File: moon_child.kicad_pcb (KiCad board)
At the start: 4 copper layers, 63.2 x 63.2 mm, 186 parts, among them J1 Motor0, J10 USB_C_Receptacle_USB2.0_14P, J2 Motor1, J3 Battery Input, J4 Micro_SD_Card_Det1, J5 Conn_01x04, J6 Conn_01x04, J7 Conn_02x05_Odd_Even, J8 Conn_01x03, J9 debug_probe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

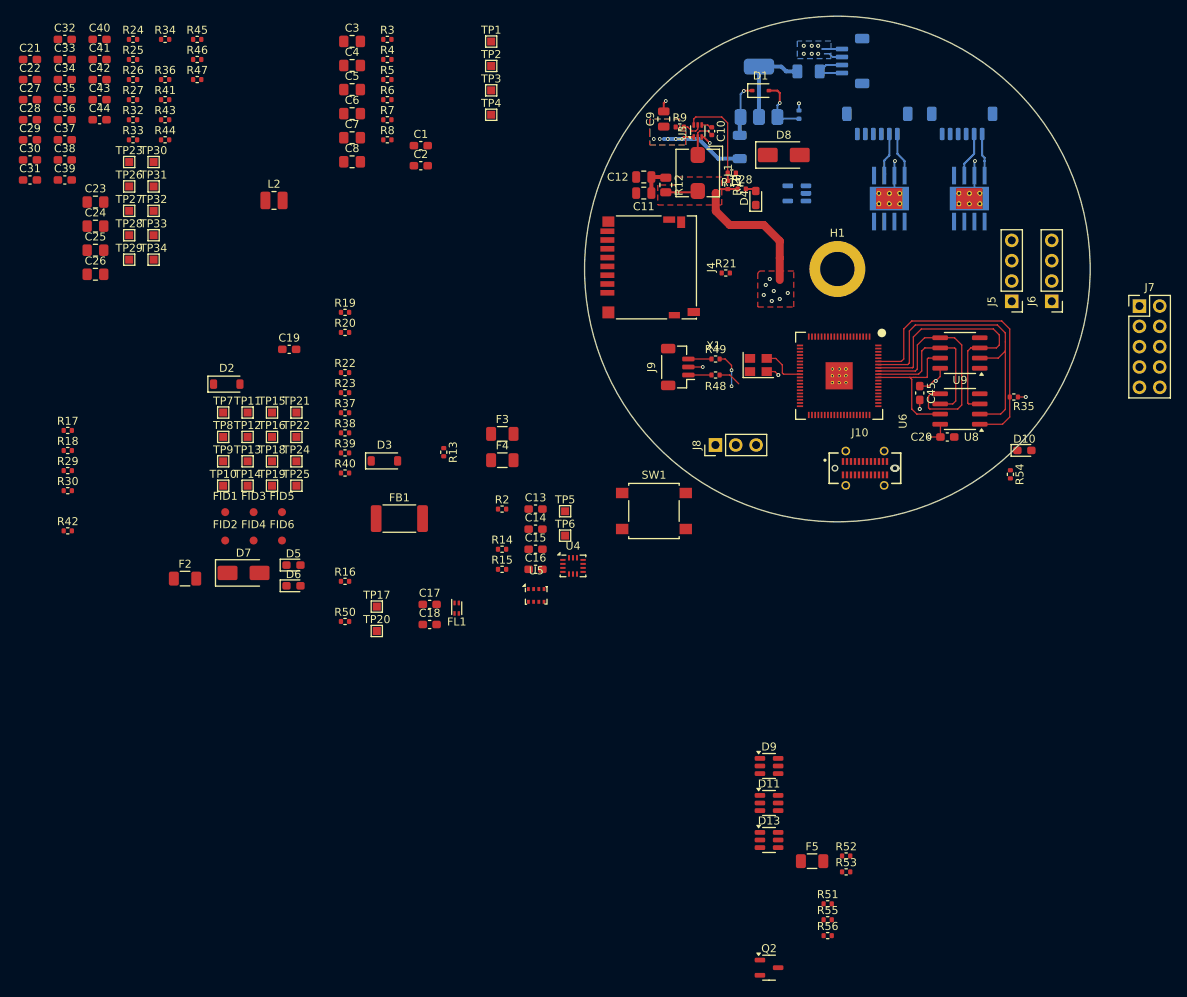
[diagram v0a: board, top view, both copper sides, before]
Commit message: GPS layout
Routed gps and motor control connections
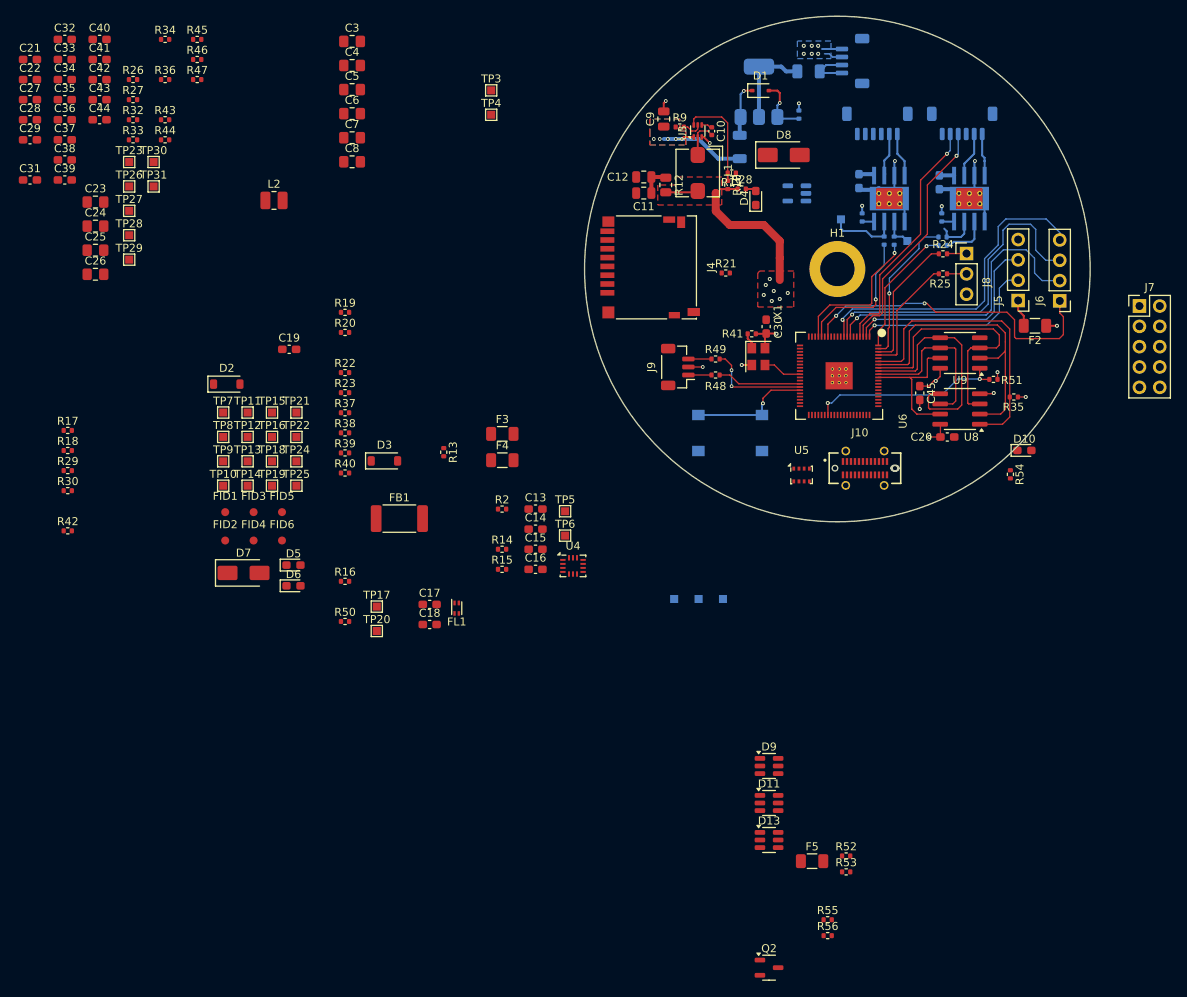
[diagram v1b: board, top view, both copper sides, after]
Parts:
- C1, C2, R3, R4, R5, R6, R7, R8, SW1, TP1, TP2, TP32, TP33, TP34: moved to B.Cu
- moved F2 110.8 mm to (183.9, 95.6), turned to 180 degrees
- moved R24 104.7 mm to (172.4, 86.6)
- moved R25 104.7 mm to (172.4, 89.1), turned to 180 degrees
- moved C30 94.4 mm to (150.3, 95.7), turned to 90 degrees
- moved TP34 82.9 mm to (144.9, 129.8), turned to -90 degrees
- moved TP33 81.9 mm to (141.8, 129.8), turned to -90 degrees
- moved TP32 81.2 mm to (138.8, 129.8), turned to -90 degrees
- moved R41 79.0 mm to (148.5, 96.6), turned to 180 degrees
- moved R5 72.1 mm to (172.3, 84.5)
- moved R6 71.8 mm to (172.4, 85.5), turned to 180 degrees
- moved R8 70.0 mm to (172.2, 82.0), turned to 90 degrees
- moved R51 68.7 mm to (178.7, 102.3), turned to 180 degrees
- moved R4 67.3 mm to (166.3, 85.0), turned to -90 degrees
- moved R3 67.0 mm to (165.1, 85.0), turned to 90 degrees
- moved C2 64.9 mm to (171.9, 77.7), turned to -90 degrees
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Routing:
- net /connectors+mechanical/GPS_SAFE: track 0.00 -> 41.4 mm, vias 0 -> 1
- net /connectors+mechanical/GPS_INT: track 0.00 -> 40.7 mm, vias 0 -> 1
- net /connectors+mechanical/GPS_PPS: track 0.00 -> 39.8 mm, vias 0 -> 2
- net /connectors+mechanical/GPS_RESET: track 0.00 -> 37.7 mm, vias 0 -> 1
- net /connectors+mechanical/Encoder1_A: track 0.00 -> 30.8 mm, vias 0 -> 1
- net /connectors+mechanical/Encoder1_B: track 0.00 -> 30.6 mm, vias 0 -> 1
- net /connectors+mechanical/GPS_TX: track 0.00 -> 26.6 mm, vias 0 -> 1
- net /raspi/QSPI_BK_SS: track 0.00 -> 24.3 mm, vias 0 -> 2
- net /connectors+mechanical/GPS_RX: track 0.00 -> 23.7 mm, vias 0 -> 1
- net GND: track 24.2 -> 44.1 mm, vias 14 -> 17
- net /motor drives/M1_IN1: track 0.00 -> 18.6 mm, vias 0 -> 1
- net /motor drives/M0_IN2: track 0.00 -> 18.5 mm, vias 0 -> 1
- net /motor drives/M0_IN1: track 0.00 -> 17.4 mm, vias 0 -> 1
- net /raspi/Raspi_RX: track 0.00 -> 16.9 mm
- net /motor drives/M1_IN2: track 0.00 -> 16.4 mm, vias 0 -> 1
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
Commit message: Moved passives
Lots passive routing
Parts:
- C25, FB1, U4: moved to B.Cu
- SW1: moved to F.Cu
- moved C25 102.0 mm to (166.8, 104.4), turned to -90 degrees
- moved C18 92.1 mm to (166.9, 61.9), turned to -90 degrees
- moved C17 91.9 mm to (169.5, 61.9), turned to -90 degrees
- moved FB1 86.1 mm to (170.2, 64.2)
- moved L2 81.7 mm to (166.8, 104.2), turned to -90 degrees
- moved FL1 70.7 mm to (159.2, 78.7), turned to 180 degrees
- moved U4 50.9 mm to (169.0, 98.1), turned to 180 degrees
- moved J10 0.76 mm to (163.4, 113.2)
- moved C45 0.30 mm to (169.8, 104.0)
- turned SW1 to 0 degrees
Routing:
- net /connectors+mechanical/Encoder0_A: track 0.00 -> 31.3 mm, vias 0 -> 1
- net /connectors+mechanical/Encoder0_B: track 0.00 -> 31.2 mm, vias 0 -> 1
- net /raspi/1V1: track 0.00 -> 6.55 mm, vias 0 -> 1
- net Net-(U6-VREG_LX): track 0.00 -> 3.58 mm
- net GND: track 44.1 -> 45.2 mm, vias 17 -> 19
- net /raspi/~{RESET}: vias 1 -> 0
- added copper zone on F.Cu, net GND

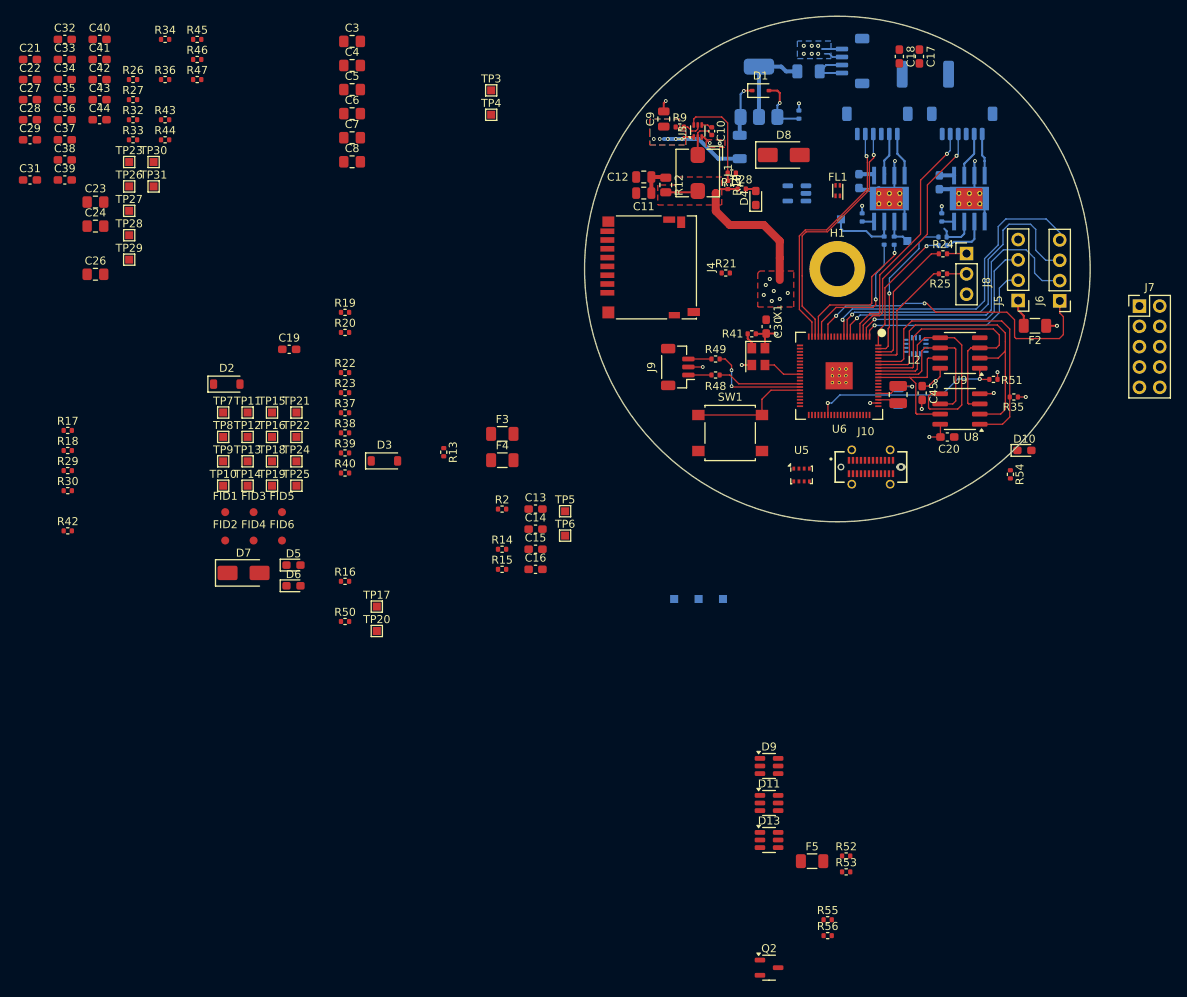
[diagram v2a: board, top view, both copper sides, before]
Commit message: Distributed caps
Remembered to add decoupling caps
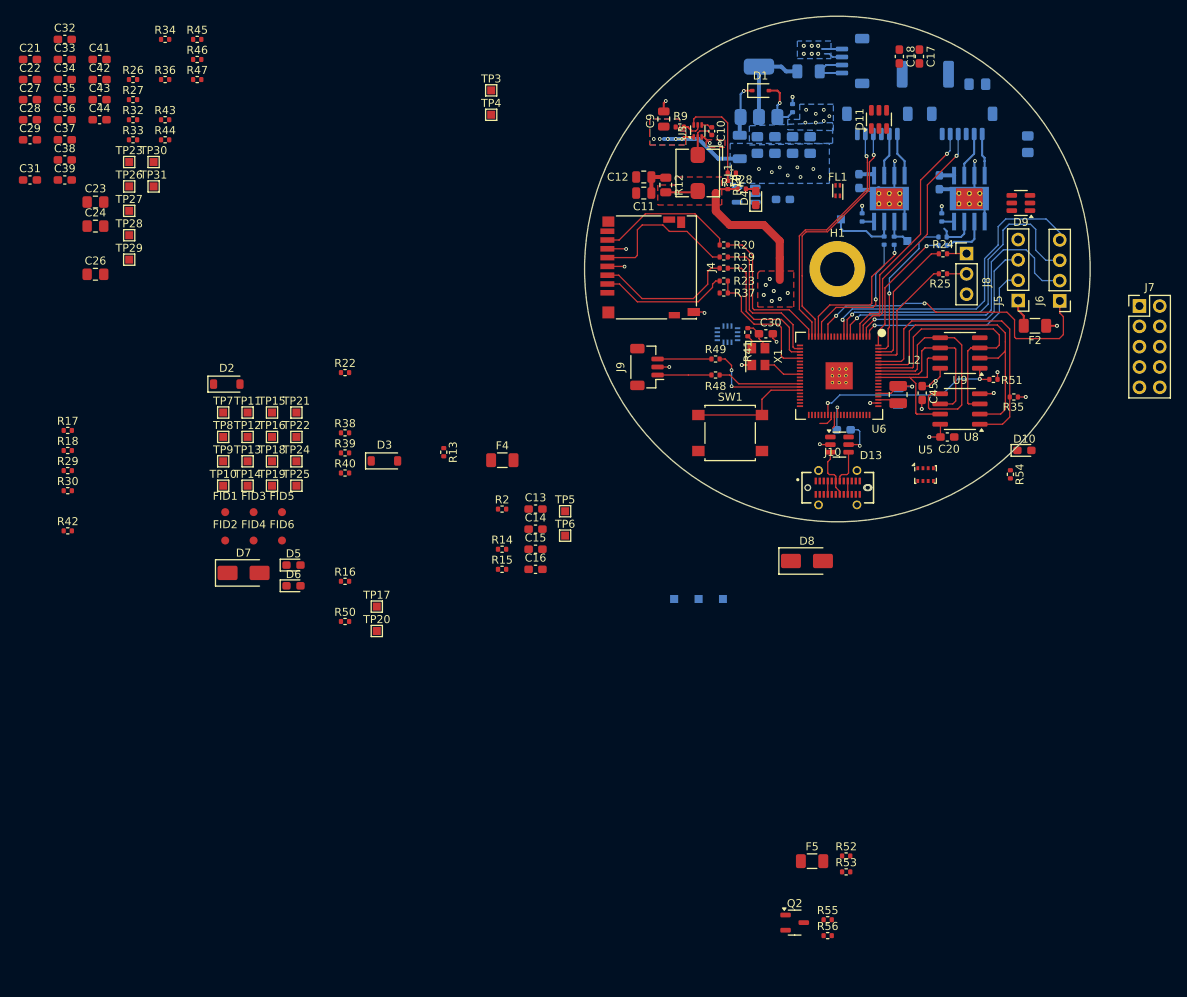
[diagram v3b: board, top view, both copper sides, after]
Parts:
- removed F3: Polyfuse_Small, Fuse:Fuse_1206_3216Metric
- C19, C3, C4, C40, C5, C6, C7, C8: moved to B.Cu
- moved C40 105.0 mm to (160.0, 108.6)
- moved D11 86.5 mm to (164.4, 69.8), turned to 90 degrees
- moved C3 85.4 mm to (183.0, 72.9), turned to -90 degrees
- moved C4 78.2 mm to (176.7, 65.4)
- moved D9 77.1 mm to (182.1, 80.2), turned to 180 degrees
- moved C19 64.5 mm to (152.4, 79.8)
- moved C5 57.7 mm to (155.8, 73.0), turned to 90 degrees
- moved C6 55.2 mm to (153.6, 73.0), turned to 90 degrees
- moved C7 52.9 mm to (151.4, 73.0), turned to 90 degrees
- moved D8 50.8 mm to (155.4, 125.0)
- moved C8 50.7 mm to (149.2, 73.0), turned to 90 degrees
- moved D13 50.2 mm to (159.5, 110.5)
- moved R37 49.7 mm to (145.0, 91.5)
- moved R23 49.4 mm to (145.0, 90.0), turned to 180 degrees
- moved R20 48.6 mm to (145.0, 85.5), turned to 180 degrees
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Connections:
- J4 pad 4: Net-(J4-VDD) -> 3v3
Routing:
- net /sensors/MCU_SDI: track 0.00 -> 19.3 mm
- net Net-(J4-CLK): track 0.00 -> 19.3 mm
- net /sensors/MCU_SCLK: track 0.00 -> 19.0 mm
- net /sensors/MCU_SDO: track 0.00 -> 17.8 mm
- net Net-(J4-CMD): track 0.00 -> 17.8 mm
- net Net-(J4-DAT0): track 0.00 -> 17.5 mm
- net /raspi/SD_CS: track 0.00 -> 17.1 mm
- net Net-(J4-DAT3/CD): track 0.00 -> 16.3 mm
- net GND: track 45.2 -> 55.6 mm, vias 19 -> 31
- net /connectors+mechanical/DP+: track 0.00 -> 6.38 mm
- net 3v3: track 38.1 -> 43.3 mm, vias 13 -> 14
- net /connectors+mechanical/DP-: track 0.00 -> 4.45 mm
- net Net-(J9-Pin_3): track 2.89 -> 6.74 mm
- net Net-(J9-Pin_1): track 2.89 -> 6.74 mm
- net Net-(F5-Pad2): track 0.00 -> 3.34 mm
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
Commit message: imu routing
updates to imu routes
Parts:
- C15, C16, R13: moved to B.Cu
- moved C16 35.4 mm to (145.1, 99.6), turned to 180 degrees
- moved R13 35.1 mm to (141.6, 96.2), turned to 0 degrees
- moved C15 32.8 mm to (141.5, 97.5), turned to 180 degrees
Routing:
- net /raspi/IMU_CS: track 0.00 -> 17.3 mm, vias 0 -> 3
- net /sensors/MCU_SDI: track 19.3 -> 30.0 mm, vias 0 -> 1
- net /sensors/MCU_SCLK: track 19.0 -> 28.2 mm, vias 0 -> 1
- net 3v3: track 43.3 -> 51.2 mm, vias 14 -> 18
- net /sensors/MCU_SDO: track 17.8 -> 25.4 mm, vias 0 -> 1
- net GND: track 55.6 -> 60.6 mm, vias 31 -> 33
- net Net-(U4-INT2/FSYNC/CLKIN): track 0.00 -> 2.37 mm

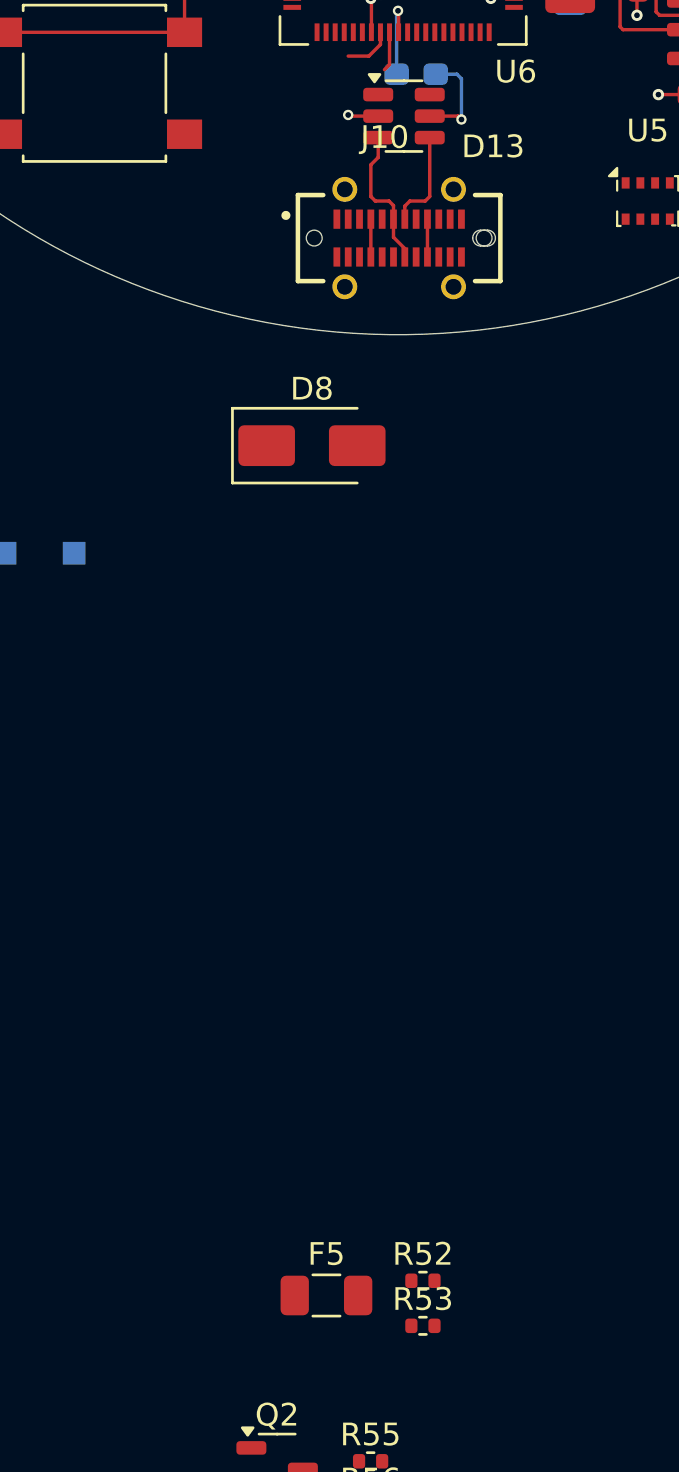
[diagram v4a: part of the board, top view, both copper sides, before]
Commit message: USB routing
Updated usb routing
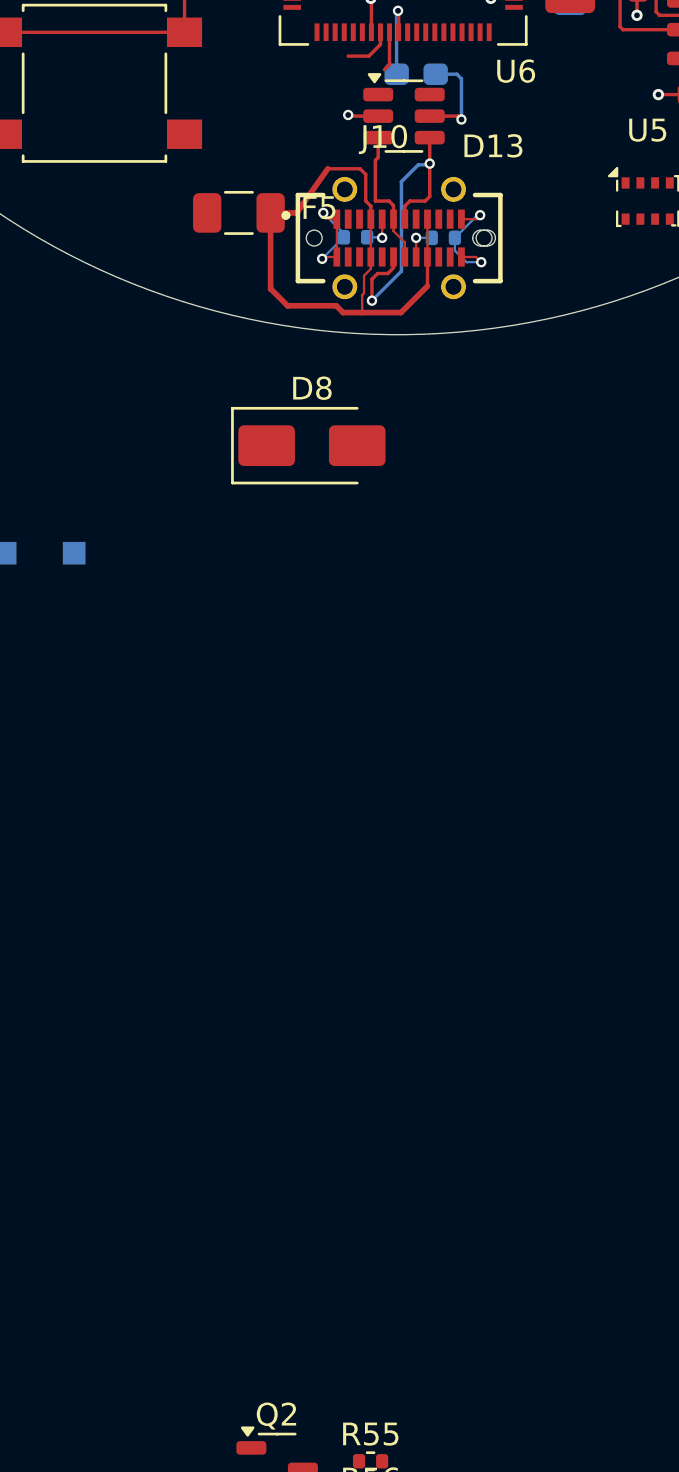
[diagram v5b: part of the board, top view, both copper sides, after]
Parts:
- R52, R53: moved to B.Cu
- moved R53 48.0 mm to (161.2, 115.8), turned to 180 degrees
- moved F5 48.0 mm to (152.2, 114.7)
- moved R52 46.2 mm to (157.3, 115.8)
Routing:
- net Net-(F5-Pad2): track 3.34 -> 25.8 mm
- net GND: track 60.6 -> 71.9 mm, vias 33 -> 37
- net /connectors+mechanical/DP-: track 4.45 -> 14.4 mm, vias 0 -> 2
- net Net-(J10-CC2): track 0.00 -> 1.53 mm, vias 0 -> 1
- net Net-(J10-CC1): track 0.00 -> 1.50 mm, vias 0 -> 1
